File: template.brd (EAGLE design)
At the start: 124.5 x 55.9 mm, 62 parts, among them J1 RJ45KEYSTONE-942, J2 JTAG_ARM_10PIN, J3 APP_2POS_CONFIG12V_HORIZ, U1 TM4C1294NCPDT, U2 HX1198FNL, U3 SLVU2.8-4, U4 OKI-78SR-5/1.5-W36HC, U5 TPS73733DCQ, Y1 NX3225GA, Y2 CRYATL_32K_SMD

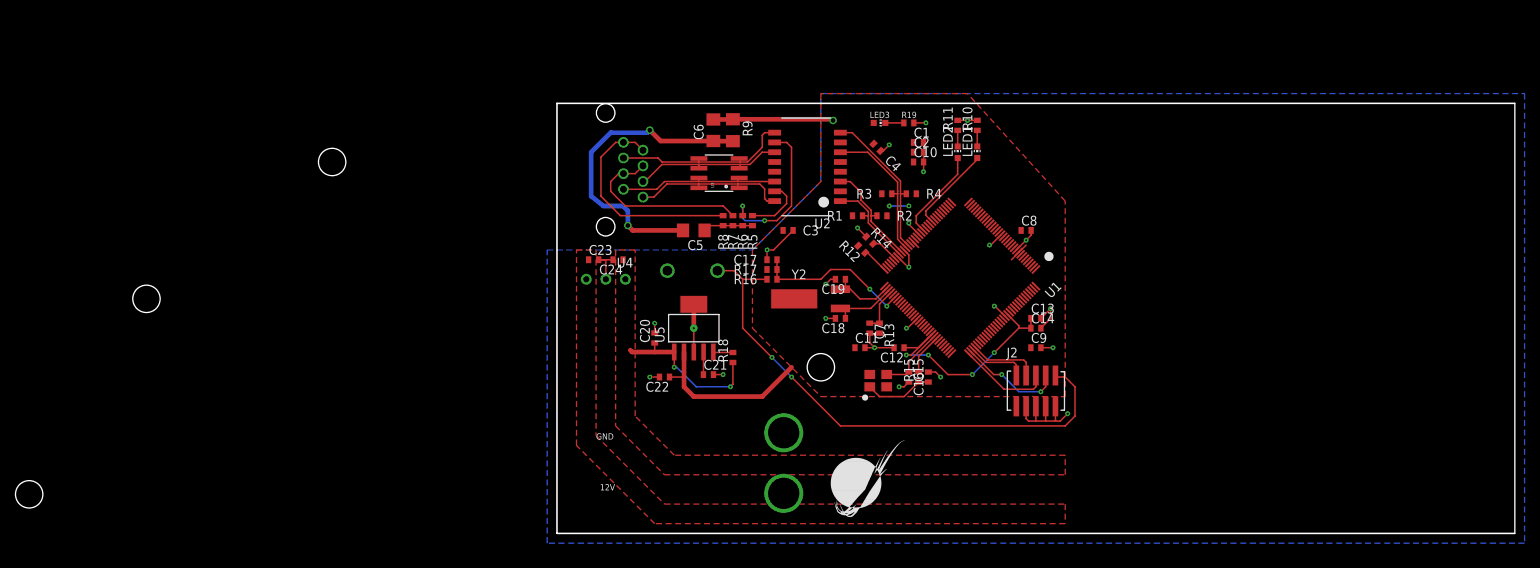
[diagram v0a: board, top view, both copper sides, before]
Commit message: Made Components bigger, and rearrageneged for solderability
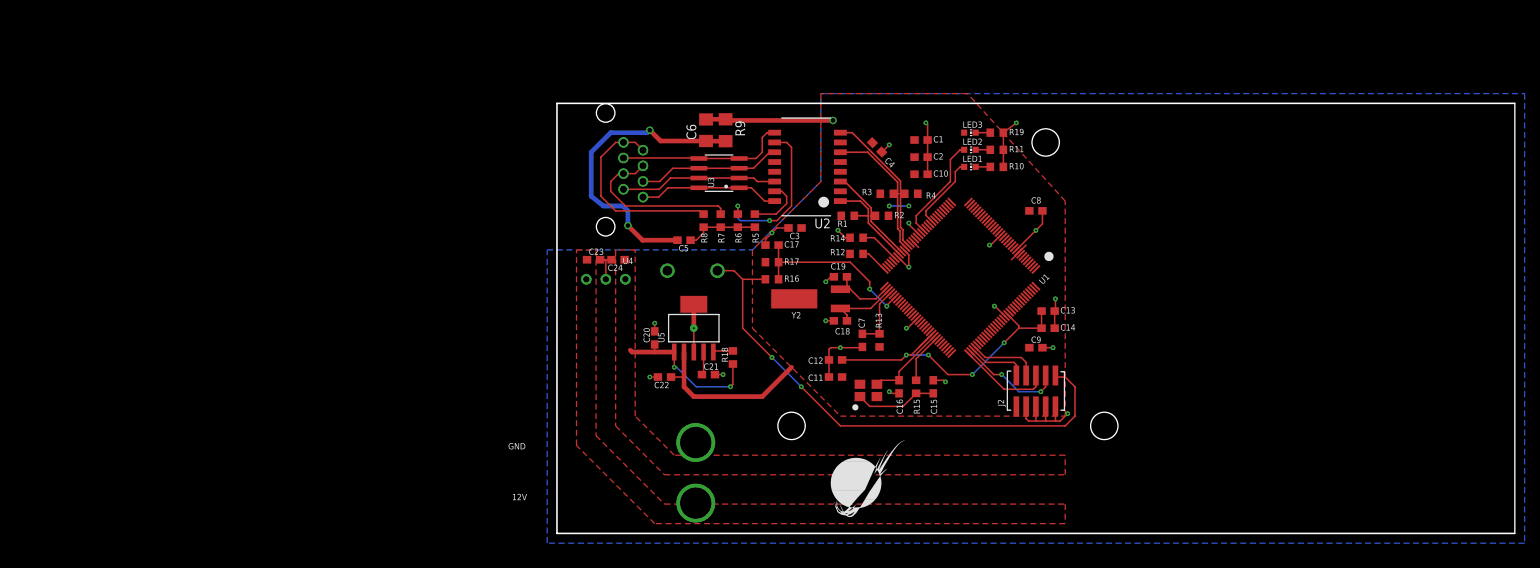
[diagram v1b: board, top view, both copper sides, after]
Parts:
- removed U$5: MOUNTING_HOLE#6, MRDT-Hardware:#6_SCREW
- C1, C10, C11, C12, C13, C14, C15, C17, C18, C19, C2, C20, C21, C22, C23, C24, C3, C4, C7, C8, C9: device resistor:C0402 -> resistor:C0603
- C16: device rcl:C0402 -> resistor:C0603
- C5: device resistor:C1206 -> resistor:C0603
- LED1, LED2: value (none) -> GREEN
- LED3: value (none) -> ORANGE
- R1: device resistor:R0402 -> rcl:R0603
- R10, R11, R12, R13, R14, R15, R16, R17, R18, R2, R3, R4, R5, R6, R7, R8: device resistor:R0402 -> resistor:R0603
- R19: value 1k -> 330; device resistor:R0402 -> resistor:R0603
- moved U$2 140.0 mm to (71.1, 14.0)
- moved U$4 118.6 mm to (63.5, 50.8)
- moved LED3 11.8 mm to (53.7, 52.1)
- moved J3 11.5 mm to (-10.2, 0.00)
- moved R19 11.5 mm to (57.1, 52.1)
- moved U$3 8.52 mm to (30.5, 14.0)
- moved C12 8.41 mm to (36.2, 22.5)
- moved R11 5.99 mm to (57.1, 49.8), turned to 0 degrees
- moved R10 5.97 mm to (57.1, 47.6), turned to 0 degrees
- moved C11 4.96 mm to (36.2, 20.3), turned to 180 degrees
- moved C8 2.84 mm to (62.2, 41.9)
- moved R8 2.54 mm to (19.1, 40.6)
- moved LED1 2.13 mm to (53.7, 47.6), turned to 270 degrees
- moved C17 1.91 mm to (27.9, 37.5)
- moved C13 1.85 mm to (63.8, 28.9)
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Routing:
- net N$16: track 32.3 -> 41.4 mm
- net GND: track 95.3 -> 102.9 mm, vias 25 -> 24
- net N$14: track 6.48 -> 9.49 mm
- net N$13: track 28.7 -> 26.1 mm
- net N$10: track 5.85 -> 8.19 mm
- net N$6: track 20.5 -> 18.3 mm
- net N$20: track 21.0 -> 23.1 mm
- net N$21: track 8.93 -> 10.8 mm
- net EN0LED1: track 12.0 -> 13.7 mm
- net N$18: track 9.05 -> 10.7 mm
- net N$7: track 23.8 -> 22.2 mm
- net N$19: track 3.65 -> 5.30 mm
- net EN0LED0: track 11.4 -> 9.81 mm
- net EN0TXO_P: track 12.2 -> 13.4 mm
- net N$11: track 23.5 -> 22.3 mm
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
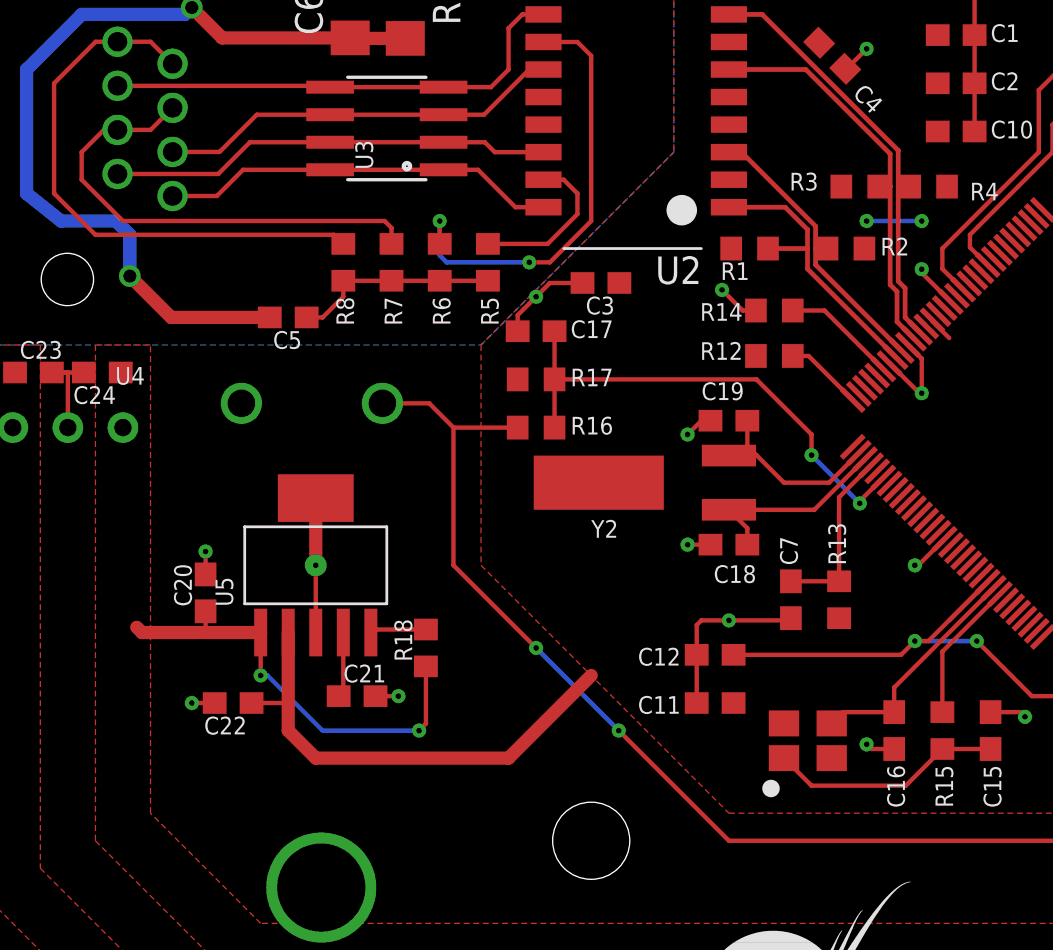
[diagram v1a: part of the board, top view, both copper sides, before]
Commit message: Replaced Pushbutton with tactile button
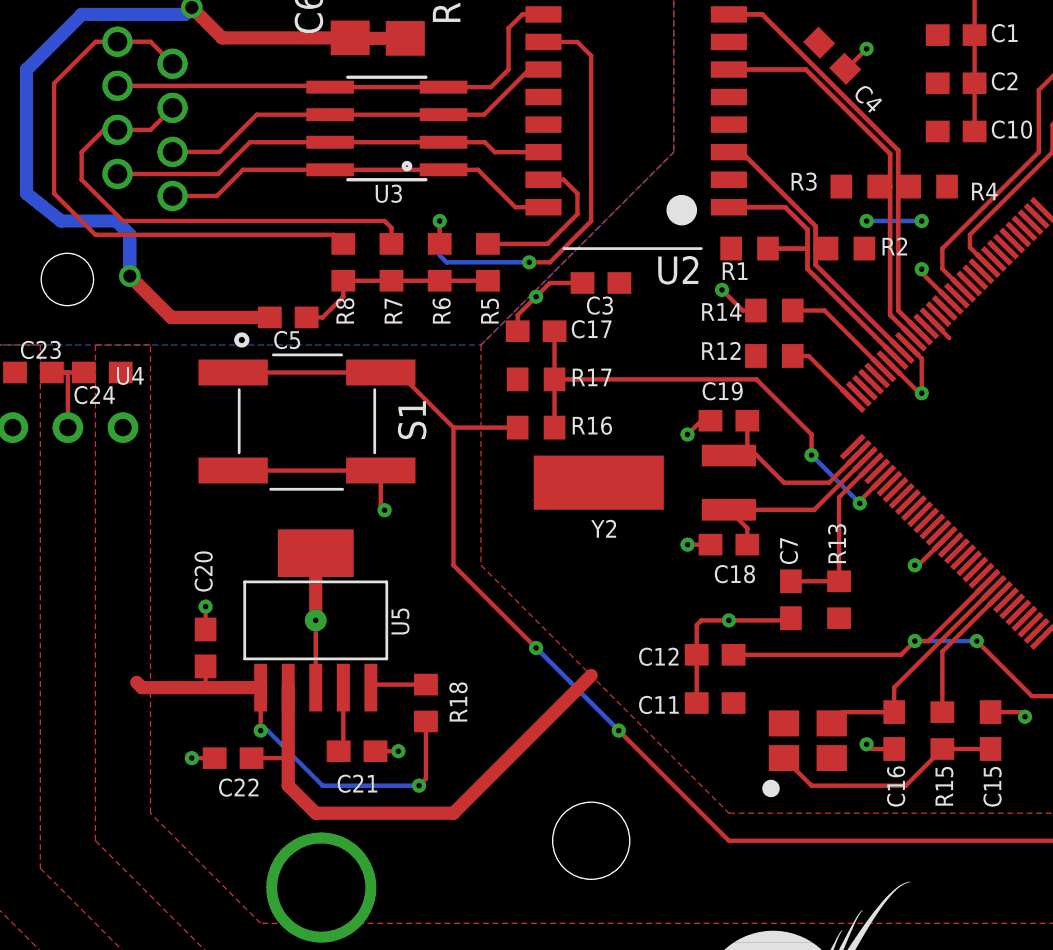
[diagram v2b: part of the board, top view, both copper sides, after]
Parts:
- S1: value PUSHBUTTONVERT -> SWITCH_TACTILE; device MRDT-UserInput:APEM-MJTP1243 -> MRDT-UserInput:SWITCH_6MM_6MM_TE_CON_SMD
- moved S1 3.24 mm to (14.0, 35.6), turned to 270 degrees
- moved U5 2.54 mm to (17.8, 24.1)
- moved C20 2.54 mm to (12.7, 22.9)
- moved C21 2.54 mm to (19.7, 18.1)
- moved C22 2.54 mm to (14.0, 17.8)
- moved R18 2.54 mm to (22.9, 20.3)
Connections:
- net !RESET: now also S1.P$3, S1.P$4; no longer S1.P$2
- net GND: now also S1.P$2
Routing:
- net GND: track 102.9 -> 111.6 mm, vias 24 -> 25
- net !RESET: track 69.0 -> 76.4 mm
- net +3V3: track 28.7 -> 29.8 mm

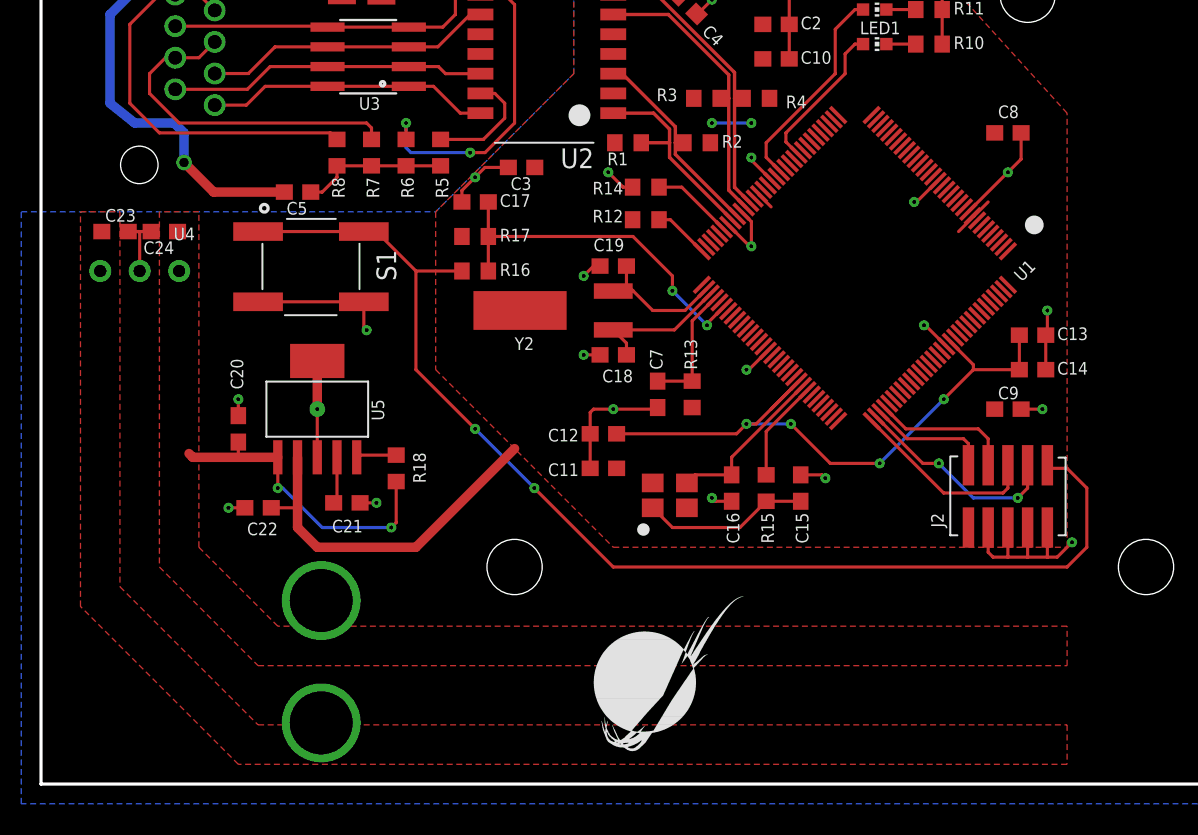
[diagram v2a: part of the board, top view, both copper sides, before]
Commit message: Added TX and RX for Serial Debugging and cleaned a little
Connected PA0 and PA1 to Arm connector for serial debugging
Added Board Info Text
Updated Libraries
renamed default nets for easier copying
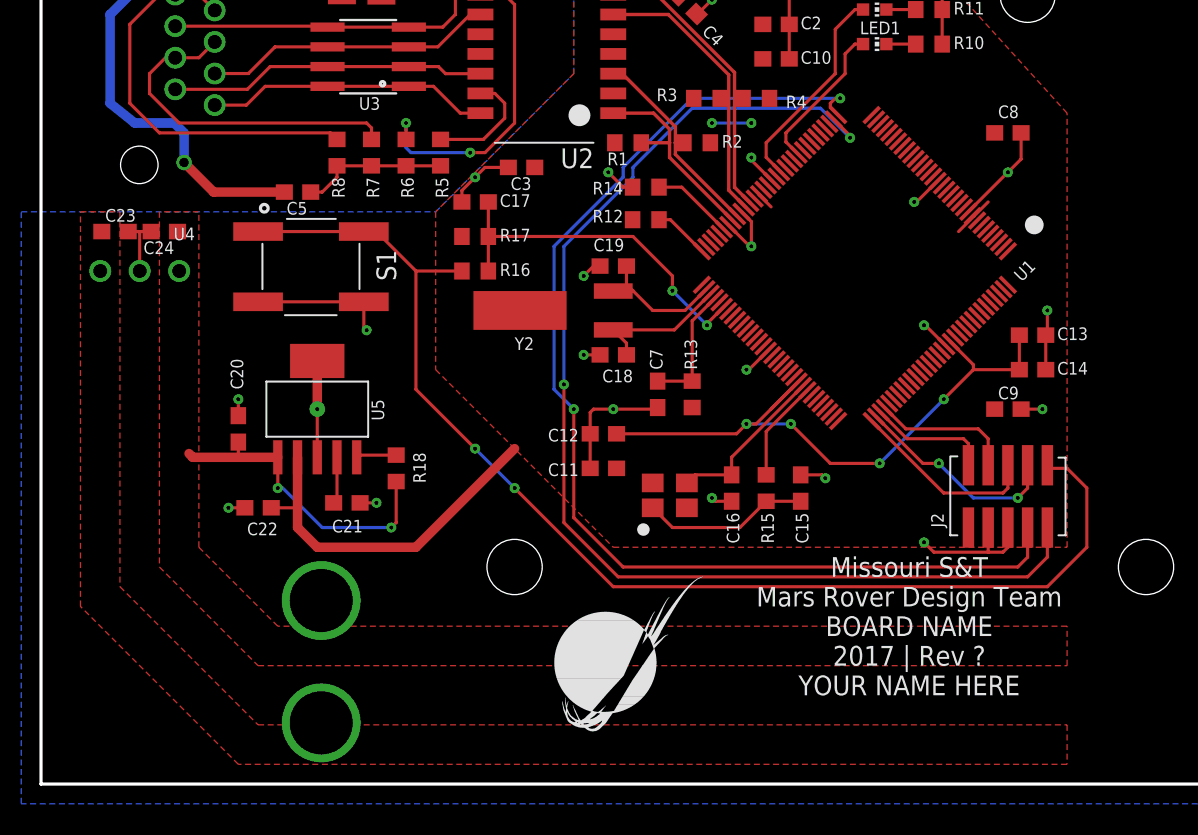
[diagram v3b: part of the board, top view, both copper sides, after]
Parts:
- moved U$1 2.84 mm to (33.0, 2.54)
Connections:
- net N$1 renamed N_$1
- net N$10 renamed N_$10
- net N$11 renamed N_$11
- net N$12 renamed N_$12
- net N$13 renamed N_$13
- net N$14 renamed N_$14
- net N$15 renamed N_$15
- net N$16 renamed N_$16
- net N$17 renamed N_$17
- net N$18 renamed N_$18
- net N$19 renamed N_$19
- net N$20 renamed N_$20
- net N$21 renamed N_$21
- net N$22 renamed N_$22
- net N$23 renamed N_$23
- net N$25 renamed N_$25
- net N$26 renamed N_$26
- net N$27 renamed N_$27
- net N$3 renamed N_$3
- net N$4 renamed N_$4
- net N$5 renamed N_$5
- net N$6 renamed N_$6
- net N$7 renamed N_$7
- net N$8 renamed N_$8
- net N$9 renamed N_$9
- removed net PA0: U1.P$33
- removed net PA1: U1.P$34
- new net RX: J2.P7, U1.P$33
- new net TX: J2.P9, U1.P$34
- net GND: no longer J2.P7, J2.P9
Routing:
- net TX: track 0.00 -> 77.6 mm, vias 0 -> 2
- net RX: track 0.00 -> 75.1 mm, vias 0 -> 2
- net GND: track 111.6 -> 107.0 mm
- net !RESET: track 76.4 -> 78.2 mm
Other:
- board text added: "Missouri S&T Mars Rover Design Team BOARD NAME 2017 | Rev ? YOUR NAME HERE"
